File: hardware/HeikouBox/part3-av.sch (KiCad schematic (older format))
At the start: 55 parts, among them J301 DB15_Female_HighDensity_Mount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, J302 AudioJack3_SwitchTR, Q301 MMBT3904, Q302 MMBT3904, Q303 MMBT3904, Q304 MMBT3904, Q305 MMBT3904, Q306 MMBT3904, Q307 MMBT3904

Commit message: Replace MCU with blue pill, tidy up
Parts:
- removed RN301, RN302, RN303, RN304, RN305, RN306, RN307, RN308, RN309, RN310, RN311, RN312, RN313: 2K2, Resistor_SMD:R_Array_Convex_4x0603, symbol Device:R_Pack04_Split
- added R323, R324, R325, R326, R327, R328, R329, R330, R331, R332, R333, R334, R335, R336, R337, R338, R339, R340, R341, R342, R343, R344, R345, R346, R347, R348, R349, R350, R351, R352, R353, R354, R355, R356, R357, R358, R359, R360, R361, R362, R363, R364, R365, R366, R367, R368, R369, R?: 2K2, Resistor_SMD:R_0603_1608Metric_Pad1.05x0.95mm_HandSolder, symbol Device:R
- C303, C304: value 10n -> 4n7
- R313, R314: value 1K -> 2K2
- renumbered Q305 to Q304, Q304 to Q305, R317 to R315, R318 to R316, R319 to R317, R320 to R318, R321 to R319, R322 to R320, R315 to R321, R316 to R322
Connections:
- wire segments 234 -> 257
- no-connect marks 14 -> 6
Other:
- note added: "DAC resistors should be same batch for value matching"
- note removed: "DAC resistor arrays should be same batch!\nResistors arranged for best layout"
- note removed: "Place near audio buffers"
- note removed: "Place near video DAC buffers"
- moved on the sheet: C301, C302, C303, C304, C305, C306, C307, C308, J301, J302, Q301, Q302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

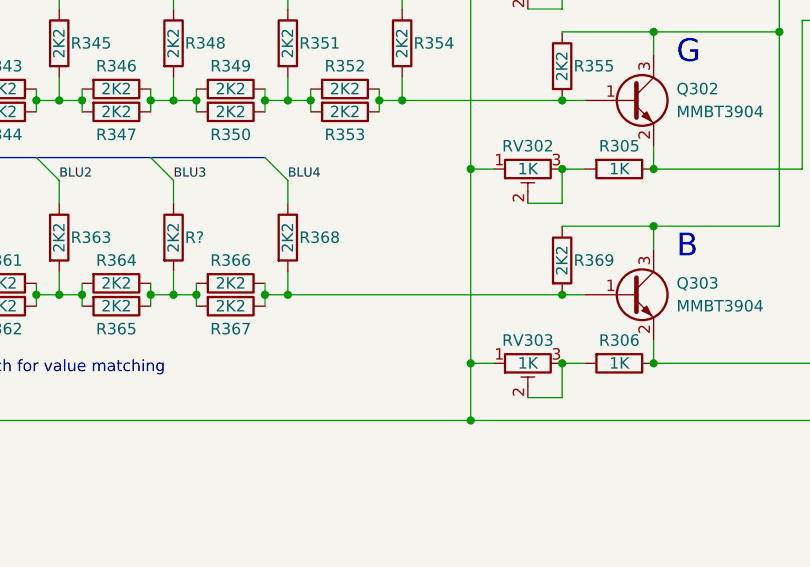
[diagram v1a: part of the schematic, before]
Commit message: Fix DRC, make netlist
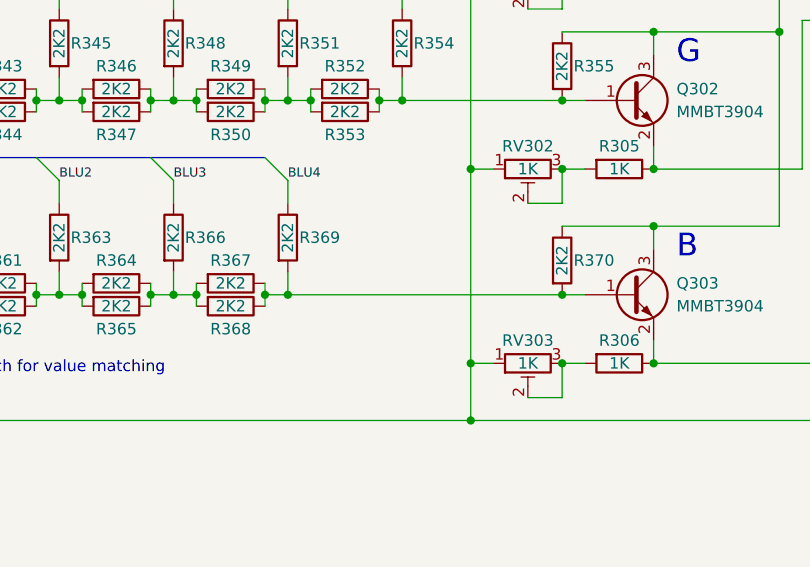
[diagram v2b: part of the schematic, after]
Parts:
- gave numbers to parts that had none: 1
- renumbered R366 to R367, R367 to R368, R368 to R369, R369 to R370
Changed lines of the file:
@@
 $Descr A4 11693 8268
 encoding utf-8
-Sheet 2 6
+Sheet 4 6
 Title "HeikouBox Mainboard - Audio Video Interface"
 Date "2021-03-17"
@@
 P 2700 2650
 AR Path="/64A7B7D2" Ref="R?"  Part="1"
-AR Path="/62C73AC4/64A7B7D2" Ref="R?"  Part="1"
-F 0 "R?" H 2750 2650 50  0000 L CNN
+AR Path="/62C73AC4/64A7B7D2" Ref="R366"  Part="1"
+F 0 "R366" H 2750 2650 50  0000 L CNN
 F 1 "2K2" V 2700 2650 50  0000 C CNN
 F 2 "Resistor_SMD:R_0603_1608Metric_Pad1.05x0.95mm_HandSolder" V 2630 2650 50  0001 C CNN
@@
 P 2950 2850
 AR Path="/64A7B7D8" Ref="R?"  Part="1"
-AR Path="/62C73AC4/64A7B7D8" Ref="R366"  Part="1"
-F 0 "R366" V 2850 2850 50  0000 C CNN
+AR Path="/62C73AC4/64A7B7D8" Ref="R367"  Part="1"
+F 0 "R367" V 2850 2850 50  0000 C CNN
 F 1 "2K2" V 2950 2850 50  0000 C CNN
 F 2 "Resistor_SMD:R_0603_1608Metric_Pad1.05x0.95mm_HandSolder" V 2880 2850 50  0001 C CNN
@@
 P 2950 2950
 AR Path="/64A7B7DE" Ref="R?"  Part="1"
-AR Path="/62C73AC4/64A7B7DE" Ref="R367"  Part="1"
-F 0 "R367" V 3050 2950 50  0000 C CNN
+AR Path="/62C73AC4/64A7B7DE" Ref="R368"  Part="1"
+F 0 "R368" V 3050 2950 50  0000 C CNN
 F 1 "2K2" V 2950 2950 50  0000 C CNN
 F 2 "Resistor_SMD:R_0603_1608Metric_Pad1.05x0.95mm_HandSolder" V 2880 2950 50  0001 C CNN
@@
 P 3200 2650
 AR Path="/64A7B7E4" Ref="R?"  Part="1"
-AR Path="/62C73AC4/64A7B7E4" Ref="R368"  Part="1"
-F 0 "R368" H 3250 2650 50  0000 L CNN
+AR Path="/62C73AC4/64A7B7E4" Ref="R369"  Part="1"
+F 0 "R369" H 3250 2650 50  0000 L CNN
 F 1 "2K2" V 3200 2650 50  0000 C CNN
 F 2 "Resistor_SMD:R_0603_1608Metric_Pad1.05x0.95mm_HandSolder" V 3130 2650 50  0001 C CNN
@@
 P 4400 2750
 AR Path="/64AEA7B7" Ref="R?"  Part="1"
-AR Path="/62C73AC4/64AEA7B7" Ref="R369"  Part="1"
-F 0 "R369" H 4450 2750 50  0000 L CNN
+AR Path="/62C73AC4/64AEA7B7" Ref="R370"  Part="1"
+F 0 "R370" H 4450 2750 50  0000 L CNN
 F 1 "2K2" V 4400 2750 50  0000 C CNN
 F 2 "Resistor_SMD:R_0603_1608Metric_Pad1.05x0.95mm_HandSolder" V 4330 2750 50  0001 C CNN

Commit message: Mostly routed board
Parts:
- added R371, R372: 100, Resistor_SMD:R_0603_1608Metric_Pad0.98x0.95mm_HandSolder, symbol Device:R
- C301, C302: footprint Capacitor_SMD:C_0603_1608Metric_Pad1.05x0.95mm_HandSolder -> Capacitor_SMD:C_1206_3216Metric_Pad1.33x1.80mm_HandSolder; symbol Device:C -> Device:CP1
- C303, C304: footprint Capacitor_SMD:C_0603_1608Metric_Pad1.05x0.95mm_HandSolder -> Capacitor_SMD:C_0603_1608Metric_Pad1.08x0.95mm_HandSolder
- C305, C306, C307, C308: footprint Capacitor_SMD:C_0603_1608Metric_Pad1.05x0.95mm_HandSolder -> Capacitor_SMD:C_0805_2012Metric_Pad1.18x1.45mm_HandSolder
- J302: footprint KSK_HeikouBox:Jack_3.5mm_PJ307_Horizontal_NoHoles -> KSK_HeikouBox:Jack_3.5mm_PJ307_Horizontal
- R301, R302, R303, R304, R305, R306, R307, R308, R309, R310, R311, R312, R313, R314, R315, R316, R319, R320, R321, R322, R323, R324, R325, R326, R327, R328, R329, R330, R331, R332, R333, R334, R335, R336, R337, R338, R339, R340, R341, R342, R343, R344, R345, R346, R347, R348, R349, R350, R351, R352, R353, R354, R355, R356, R357, R358, R359, R360, R361, R362, R363, R364, R365, R366, R367, R368, R369, R370: footprint Resistor_SMD:R_0603_1608Metric_Pad1.05x0.95mm_HandSolder -> Resistor_SMD:R_0603_1608Metric_Pad0.98x0.95mm_HandSolder
- R317, R318: value 10K -> 4K7; footprint Resistor_SMD:R_0603_1608Metric_Pad1.05x0.95mm_HandSolder -> Resistor_SMD:R_0603_1608Metric_Pad0.98x0.95mm_HandSolder
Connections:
- net 5V: no longer C301.1, C302.1, Q301.3 (C), Q302.3 (C), Q303.3 (C), Q306.3 (C), Q307.3 (C), R317.1, R318.1, R337.1, R355.1, R370.1
- net at J302.T, J302.TN: now also R371.1; no longer C307.1
- net at Q302.2 (E), R302.2: no longer R305.1
- net at Q302.1 (B), R354.2, R355.2: now also R305.1, R352.2, R353.2; no longer R352.1, R353.1
- net at Q303.2 (E), R303.2: no longer R306.1
- net at Q303.1 (B), R369.2, R370.2: now also R306.1, R367.2, R368.2; no longer R367.1, R368.1
- net at Q301.1 (B), R336.2, R337.2: now also R304.1, R334.2, R335.2; no longer R334.1, R335.1
- net at Q301.2 (E), R301.2: no longer R304.1
- net at J302.R, J302.RN: now also R372.1; no longer C308.1
- net at R323.2, R324.1: now also R325.1, R326.1; no longer R325.2, R326.2
- net at R338.2, R339.1: now also R340.1, R341.1; no longer R340.2, R341.2
- net at R356.2, R357.1: now also R358.1, R359.1; no longer R358.2, R359.2
- new net: C307.1, R371.2
- new net: C308.1, R372.2
- new net: R325.2, R326.2, R327.2, R328.1, R329.1
- new net: R328.2, R329.2, R330.2, R331.1, R332.1
- new net: R331.2, R332.2, R333.2, R334.1, R335.1
- new net: R340.2, R341.2, R342.2, R343.1, R344.1
- new net: R343.2, R344.2, R345.2, R346.1, R347.1
- new net: R346.2, R347.2, R348.2, R349.1, R350.1
- new net: R349.2, R350.2, R351.2, R352.1, R353.1
- new net: R358.2, R359.2, R360.2, R361.1, R362.1
- new net: R361.2, R362.2, R363.2, R364.1, R365.1
- new net: R364.2, R365.2, R366.2, R367.1, R368.1
- new net 3V3: C301.1, C302.1, Q301.3 (C), Q302.3 (C), Q303.3 (C), Q306.3 (C), Q307.3 (C), R317.1, R318.1, R337.1, R355.1, R370.1
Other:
- moved on the sheet: C307, C308, J301, J302, Q304, Q305, R301, R302, R303, R304, R305, R306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

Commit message: Mainboard v0.1 PCB ready for export
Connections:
- net 3V3: now also R311.1, R312.1
- net GND: now also R309.2, R310.2; no longer R309.1, R310.1
- net LSIGMA: now also R313.1; no longer R313.2
- net NHSYNC: now also R307.1; no longer R307.2
- net NVSYNC: now also R308.1; no longer R308.2
- net RSIGMA: now also R314.1; no longer R314.2
- net at Q307.2 (E), R322.1: now also C308.1; no longer C308.2
- net at Q307.1 (B), R318.2, R320.1: now also C306.2; no longer C306.1
- net at Q306.1 (B), R317.2, R319.1: now also C305.2; no longer C305.1
- net at R315.1: now also C303.1, R313.2; no longer C305.2
- net at Q306.2 (E), R321.1: now also C307.1; no longer C307.2
- net at R371.2: now also J302.T, J302.TN; no longer C307.1
- net at J301.14, Q305.3 (C): now also R312.2; no longer R312.1
- net at J301.13, Q304.3 (C): now also R311.2; no longer R311.1
- net at R302.1: now also Q302.2 (E); no longer J301.2
- net at R302.2: now also J301.2; no longer Q302.2 (E)
- net at R303.1: now also Q303.2 (E); no longer J301.3
- net at R303.2: now also J301.3; no longer Q303.2 (E)
- net at Q301.2 (E): now also R301.1; no longer R301.2
- net at J301.1: now also R301.2; no longer R301.1
- net at R316.1: now also C304.1, R314.2; no longer C306.2
- net at R372.2: now also J302.R, J302.RN; no longer C308.1
- removed net 5V: R311.2, R312.2
- new net: C305.1, R315.2
- new net: C307.2, R371.1
- new net: Q304.1 (B), R307.2, R309.1
- new net: Q305.1 (B), R308.2, R310.1
- new net: C306.1, R316.2
- new net: C308.2, R372.1
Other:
- note added: "Bulk capacitor\nfor VGA buffers"
- note added: "Bulk capacitor\nfor audio buffers"
- moved on the sheet: C301, C302, C303, C304, C305, C306, C307, C308, J301, J302, Q301, Q302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

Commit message: Tidy up power nets
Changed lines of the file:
@@
 Wire Wire Line
 	6000 2100 7400 2100
-Text HLabel 5500 3500 1    40   Input ~ 0
-3V3
-Text HLabel 7400 1400 1    40   Input ~ 0
-3V3
-Text HLabel 1000 4500 3    40   Input ~ 0
+Text HLabel 700  5700 0    40   Input ~ 0
 GND
 Wire Wire Line
@@
 	-1   0    0    -1
 $EndComp
-Text HLabel 6200 3000 3    40   Input ~ 0
-GND
-Text HLabel 5200 2700 3    40   Input ~ 0
-GND
-Wire Wire Line
-	5200 2700 5200 2600
-Connection ~ 5200 2600
 Wire Wire Line
 	4300 2200 4300 2300
-Text HLabel 4300 2200 1    40   Input ~ 0
-3V3
 Connection ~ 4300 2300
-Text HLabel 5500 4000 3    40   Input ~ 0
-GND
 Wire Wire Line
 	5500 4000 5500 3900
-Text HLabel 3900 2000 3    40   Input ~ 0
-GND
-Wire Wire Line
-	1000 4500 1000 4400
-Text HLabel 1000 1700 3    40   Input ~ 0
-GND
-Wire Wire Line
-	1000 1700 1000 1600
+Wire Wire Line
+	700  5700 800  5700
 Connection ~ 3900 1600
 Connection ~ 3900 4000
@@
 	1    0    0    -1
 $EndComp
-Text HLabel 3900 4800 3    40   Input ~ 0
-GND
 Wire Wire Line
 	4050 4400 4050 4550
@@
 Wire Wire Line
 	4300 3600 4300 3700
-Text HLabel 4300 3600 1    40   Input ~ 0
-3V3
 $Comp
 L Device:R R?
@@
 Wire Wire Line
 	4300 900  4300 1000
-Connection ~ 4300 900
 Wire Wire Line
 	3900 900  4300 900
-Wire Wire Line
-	4300 800  4300 900
-Text HLabel 4300 800  1    40   Input ~ 0
+Text HLabel 700  5600 0    40   Input ~ 0
 3V3
 Wire Wire Line
@@
 Wire Wire Line
 	3900 2900 3900 3000
-Text HLabel 3900 3400 3    40   Input ~ 0
-GND
 Wire Wire Line
 	3900 3400 3900 3300
@@
 Wire Wire Line
 	1400 2600 1400 2650
-Wire Wire Line
-	1000 3100 1000 3000
-Text HLabel 1000 3100 3    40   Input ~ 0
-GND
 Wire Wire Line
 	3500 2100 3500 2200
@@
 	3500 2100 3400 2000
 Connection ~ 1000 1200
-Wire Wire Line
-	3900 1900 3900 2000
 $Comp
 L Device:R_POT_TRIM RV?
@@
 Wire Wire Line
 	7700 2900 7400 2900
-Connection ~ 7400 2900
-Wire Wire Line
-	7400 2900 7400 3000
 Wire Wire Line
 	6200 2300 6200 1900
@@
 Text Notes 10500 4300 0    50   ~ 0
 Bulk capacitor\nfor audio buffers
-Text HLabel 10400 4700 3    40   Input ~ 0
-GND
 Wire Wire Line
 	10400 4700 10400 4600
@@
 Wire Wire Line
 	10200 6000 10200 6100
-Text HLabel 10200 6100 3    40   Input ~ 0
-GND
-Text HLabel 8100 6300 3    40   Input ~ 0
-GND
 Wire Wire Line
 	8100 4900 8100 4800
-Text HLabel 10400 4200 1    40   Input ~ 0
-3V3
 Wire Wire Line
 	9300 5100 9300 5200
-Text HLabel 9300 5100 1    40   Input ~ 0
-3V3
 Wire Wire Line
 	9300 3700 9300 3800
@@
 Wire Wire Line
 	9300 4500 9400 4500
-Text HLabel 9300 3700 1    40   Input ~ 0
-3V3
 Wire Wire Line
 	8100 5600 8100 5800
@@
 Wire Wire Line
 	8200 5600 8100 5600
-Text HLabel 8100 4900 3    40   Input ~ 0
-GND
 Text HLabel 7700 5600 0    40   Input ~ 0
 RSIGMA
@@
 	1    0    0    -1
 $EndComp
-Text HLabel 7400 3000 3    40   Input ~ 0
-GND
 Wire Wire Line
 	3500 2600 3900 2600
+Connection ~ 3500 2600
+Text Label 800  5700 0    40   ~ 8
+GND
+Wire Wire Line
+	1000 4400 1000 4500
+Text Label 1000 4500 3    40   ~ 8
+GND
+Wire Wire Line
+	1000 1600 1000 1700
+Text Label 1000 1700 3    40   ~ 8
+GND
+Wire Wire Line
+	1000 3000 1000 3100
+Text Label 1000 3100 3    40   ~ 8
+GND
+Wire Wire Line
+	3900 1900 3900 2000
+Text Label 3900 2000 3    40   ~ 8
+GND
+Text Label 5500 4000 3    40   ~ 8
+GND
+Text Label 3900 3400 3    40   ~ 8
+GND
+Text Label 3900 4800 3    40   ~ 8
+GND
+Text Label 6200 3000 3    40   ~ 8
+GND
+Wire Wire Line
+	5700 2600 5700 2700
+Text Label 5700 2700 3    40   ~ 8
+GND
+Wire Wire Line
+	7400 2900 6500 2900
+Connection ~ 6500 2900
+Connection ~ 7400 2900
+Connection ~ 5700 2600
+Text Label 8100 6300 3    40   ~ 8
+GND
+Text Label 8100 4900 3    40   ~ 8
+GND
+Text Label 10400 4700 3    40   ~ 8
+GND
+Text Label 10200 6100 3    40   ~ 8
+GND
+Text Label 4300 800  1    40   ~ 8
+3V3
+Wire Wire Line
+	4300 800  4300 900
+Text Label 800  5600 0    40   ~ 8
+3V3
+Wire Wire Line
+	700  5600 800  5600
+Text Label 5500 3500 1    40   ~ 8
+3V3
+Text Label 4300 3600 1    40   ~ 8
+3V3
+Text Label 4300 2200 1    40   ~ 8
+3V3
+Connection ~ 4300 900
+Text Label 7400 1400 1    40   ~ 8
+3V3
+Text Label 9300 5100 1    40   ~ 8
+3V3
+Text Label 9300 3700 1    40   ~ 8
+3V3
+Text Label 10400 4200 1    40   ~ 8
+3V3
 Wire Bus Line
 	850  3400 2900 3400
@@
 Wire Bus Line
 	850  2000 3400 2000
-Connection ~ 3500 2600
 $EndSCHEMATC
